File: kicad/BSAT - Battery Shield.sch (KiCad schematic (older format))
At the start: 65 parts, among them P2 SAT POWER, P3 POWER SAMPLES, Q1 NDS8435A, SW2 SAT ON/OFF, U1 LM78L09, U2 LM78L09, U3 LM78L09, U4 LM78L09, U5 LM78L09, U6 LM78L09, U7 MAX1873REEE

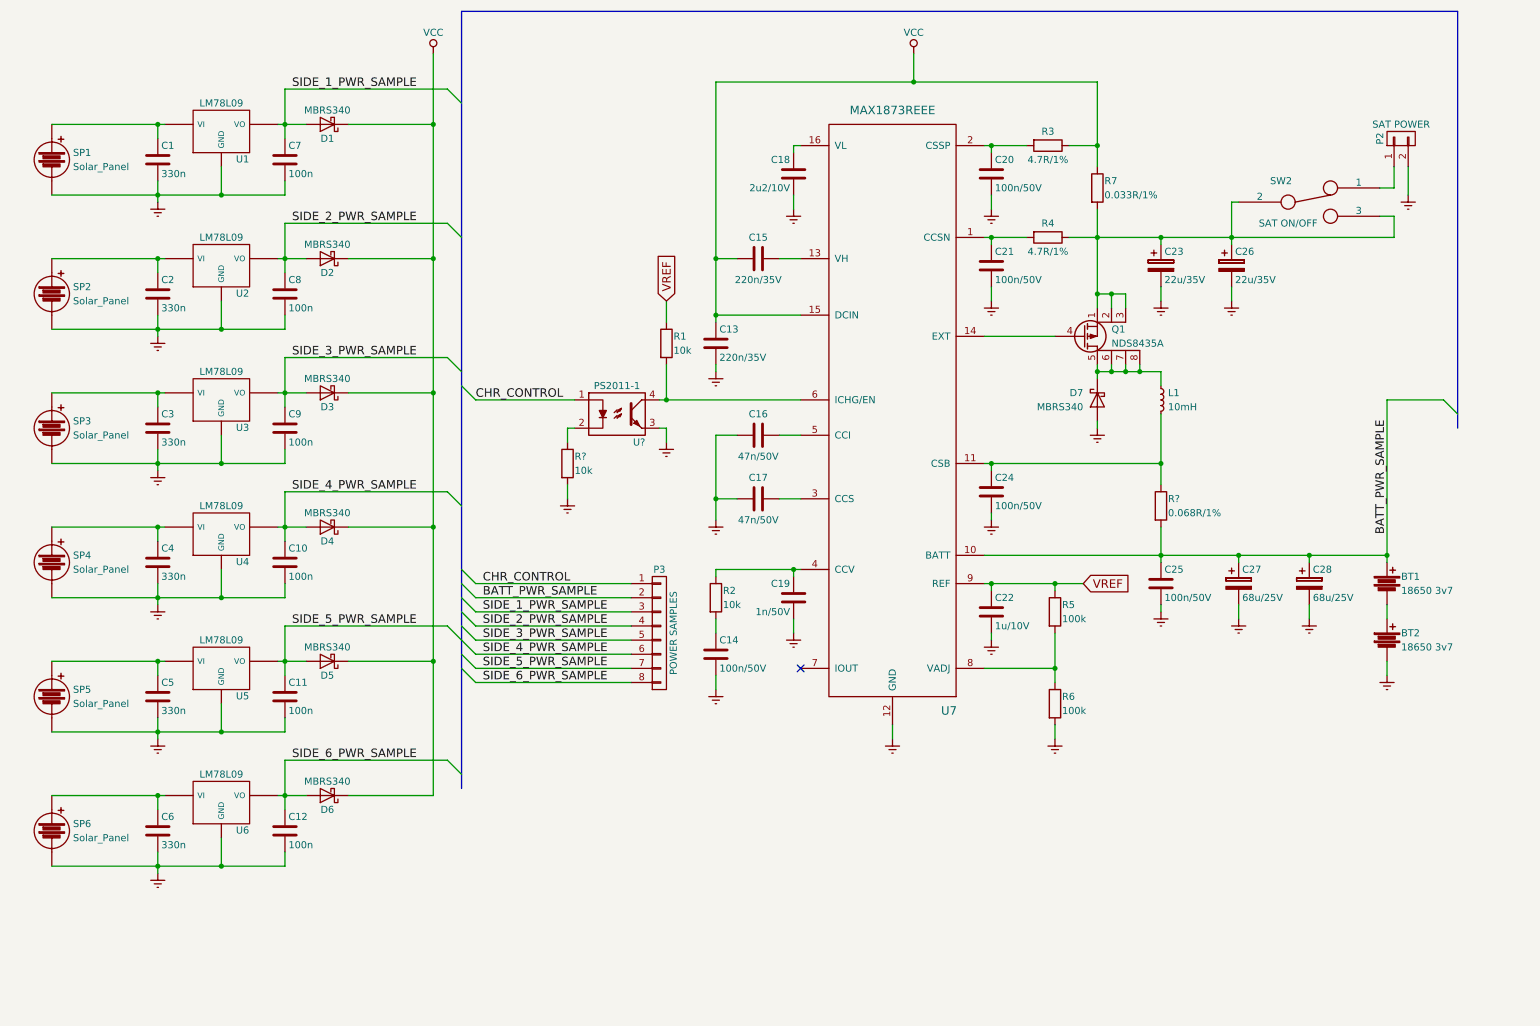
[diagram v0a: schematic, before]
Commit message: refactor(eps): Modificar el esquema del circuito para añadir los nuevos conectores.
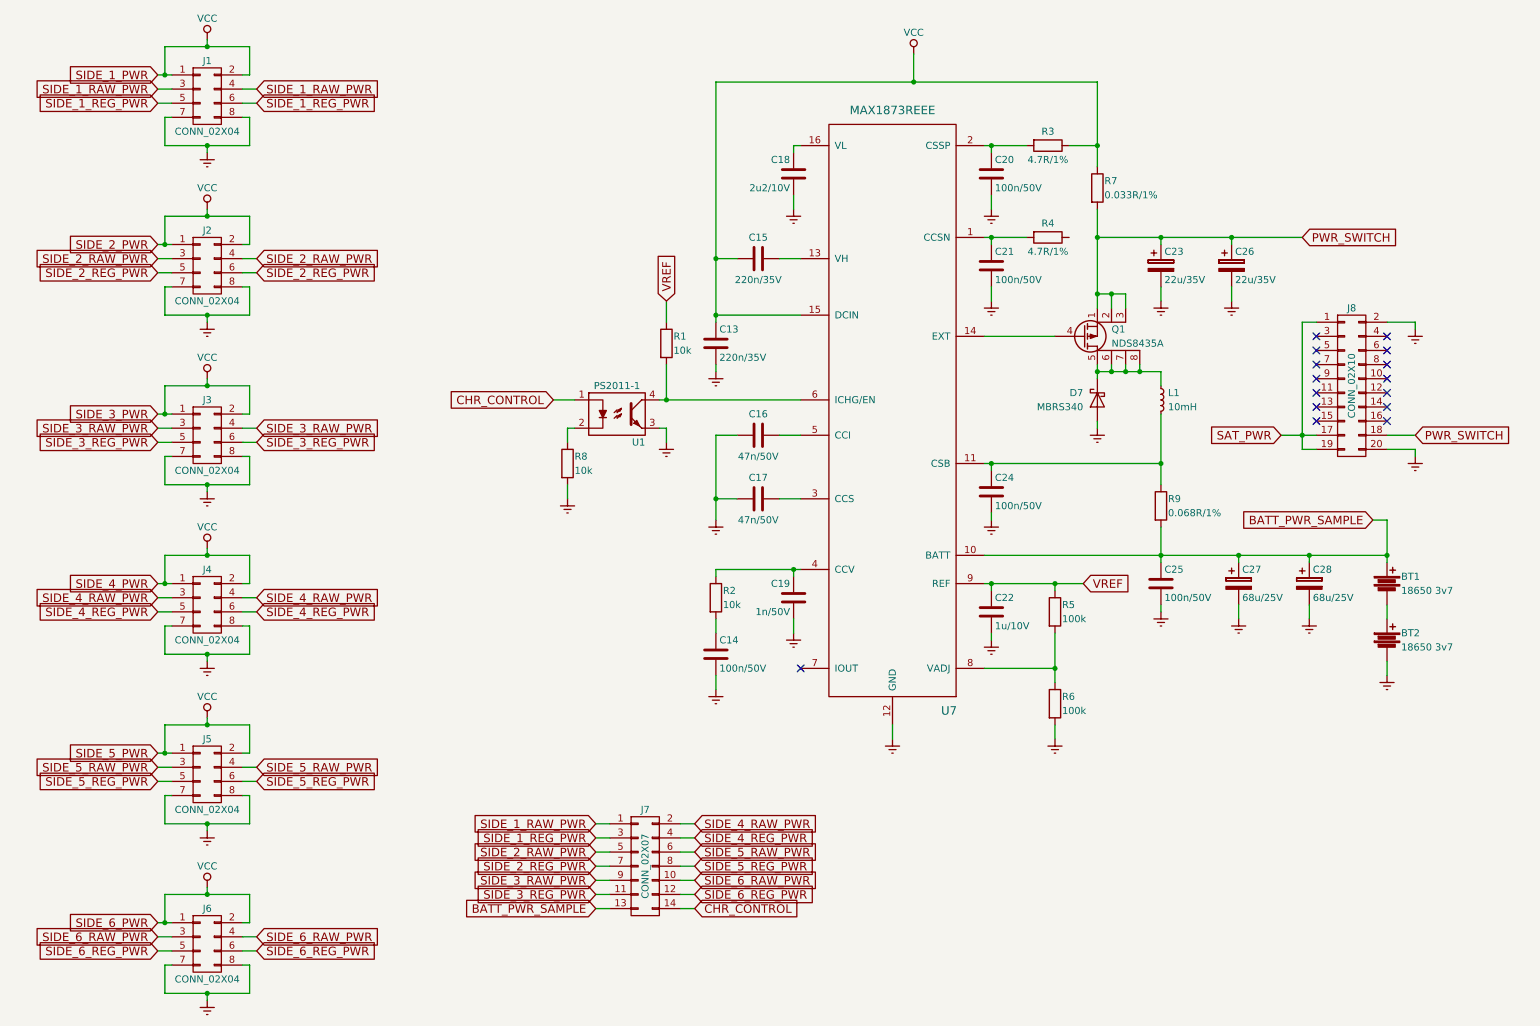
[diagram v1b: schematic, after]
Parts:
- removed C1, C2, C3, C4, C5, C6: 330n, symbol C
- removed C10, C11, C12, C7, C8, C9: 100n, symbol C
- removed D1, D2, D3, D4, D5, D6: MBRS340, symbol D_Schottky
- removed P2: SAT POWER, Pin_Headers:Pin_Header_Straight_1x02, symbol CONN_01X02
- removed P3: POWER SAMPLES, symbol CONN_01X08
- removed SP1, SP2, SP3, SP4, SP5, SP6: Solar_Panel, Pin_Headers:Pin_Header_Straight_1x02, symbol Solar_Panel
- removed SW2: SAT ON/OFF, BoscoverySAT:SWITCH-1CIR-2CON, symbol SWITCH_INV
- removed U1, U2, U3, U4, U5, U6: LM78L09, symbol LM78L09
- added J1, J2, J3, J4, J5, J6: CONN_02X04, symbol CONN_02X04
- added J7: CONN_02X07, symbol CONN_02X07
- added J8: CONN_02X10, symbol CONN_02X10
- gave numbers to parts that had none: 3
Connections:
- net BATT_PWR_SAMPLE: now also J7.13 (P13)
- net CHR_CONTROL: now also J7.14 (P14)
- net GNDREF: now also J1.7 (P7), J1.8 (P8), J2.7 (P7), J2.8 (P8), J3.7 (P7), J3.8 (P8), J4.7 (P7), J4.8 (P8), J5.7 (P7), J5.8 (P8), J6.7 (P7), J6.8 (P8), J8.2 (P2), J8.20 (P20)
- net VCC: now also J1.1 (P1), J1.2 (P2), J2.1 (P1), J2.2 (P2), J3.1 (P1), J3.2 (P2), J4.1 (P1), J4.2 (P2), J5.1 (P1), J5.2 (P2), J6.1 (P1), J6.2 (P2)
- net PWR_SWITCH: now reaches C23.1, C26.1, Q1.1 (S), Q1.2 (S), Q1.3 (S), R7.2
- net PWR_SWITCH: now also J8.18 (P18); no longer R4.1
- new net SAT_PWR: J8.1 (P1), J8.17 (P17), J8.19 (P19)
- new net SIDE_1_RAW_PWR: J1.3 (P3), J1.4 (P4), J7.1 (P1)
- new net SIDE_1_REG_PWR: J1.5 (P5), J1.6 (P6), J7.3 (P3)
- new net SIDE_2_RAW_PWR: J2.3 (P3), J2.4 (P4), J7.5 (P5)
- new net SIDE_2_REG_PWR: J2.5 (P5), J2.6 (P6), J7.7 (P7)
- new net SIDE_3_RAW_PWR: J3.3 (P3), J3.4 (P4), J7.9 (P9)
- new net SIDE_3_REG_PWR: J3.5 (P5), J3.6 (P6), J7.11 (P11)
- new net SIDE_4_RAW_PWR: J4.3 (P3), J4.4 (P4), J7.2 (P2)
- new net SIDE_4_REG_PWR: J4.5 (P5), J4.6 (P6), J7.4 (P4)
- new net SIDE_5_RAW_PWR: J5.3 (P3), J5.4 (P4), J7.6 (P6)
- new net SIDE_5_REG_PWR: J5.5 (P5), J5.6 (P6), J7.8 (P8)
- new net SIDE_6_RAW_PWR: J6.3 (P3), J6.4 (P4), J7.10 (P10)
- new net SIDE_6_REG_PWR: J6.5 (P5), J6.6 (P6), J7.12 (P12)
- no-connect marks 1 -> 15
